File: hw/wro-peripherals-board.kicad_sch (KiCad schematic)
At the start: 0 parts

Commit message: Schematic V1
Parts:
- added J1: I2C Breakout (OLED), symbol Connector:Conn_01x04_Pin
- added J2: Power-Motor Screw Terminal, symbol Connector:Conn_01x06_Pin
- added J3: GY-87 Sensor Breakout, symbol Connector:Conn_01x08_Pin
- added J4: PWM Out, symbol Connector:Conn_01x03_Pin
- added J5: PWM In, symbol Connector:Conn_01x04_Pin
- added U1: Raspberry Pi Pico, Module:RaspberryPi_Pico_Common_Unspecified, symbol MCU_Module:RaspberryPi_Pico
- added U2: TB6612FNG, Package_SO:SSOP-24_5.3x8.2mm_P0.65mm, symbol Driver_Motor:TB6612FNG
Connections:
- new net: J2.3 (Pin_3), U2.1 (AO1), U2.2 (AO1)
- new net: J2.4 (Pin_4), U2.5 (AO2), U2.6 (AO2)
- new net: J2.5 (Pin_5), U2.11 (BO1), U2.12 (BO1)
- new net: J2.6 (Pin_6), U2.7 (BO2), U2.8 (BO2)
- new net +3.3V: J1.2 (Pin_2), U1.36 (3V3), U2.20 (VCC)
- new net +5V: J3.1 (Pin_1), J5.3 (Pin_3), U1.40 (VBUS)
- new net +BATT: J2.1 (Pin_1), J4.2 (Pin_2), U2.13 (VM2), U2.14 (VM3), U2.24 (VM1)
- new net AIN1: U1.15 (GPIO11), U2.21 (AIN1)
- new net AIN2: U1.14 (GPIO10), U2.22 (AIN2)
- new net BIN1: U1.17 (GPIO13), U2.17 (BIN1)
- new net BIN2: U1.19 (GPIO14), U2.16 (BIN2)
- new net GND: J1.1 (Pin_1), J2.2 (Pin_2), J3.3 (Pin_3), J4.3 (Pin_3), J5.4 (Pin_4), U1.13 (GND), U1.18 (GND), U1.23 (GND), U1.28 (GND), U1.3 (GND), U1.38 (GND), U1.8 (GND), U2.10 (PGND2), U2.18 (GND), U2.3 (PGND1), U2.4 (PGND1), U2.9 (PGND2)
- new net PWMA: U1.12 (GPIO9), U2.23 (PWMA)
- new net PWMB: U1.20 (GPIO15), U2.15 (PWMB)
- new net RX_S: J5.2 (Pin_2), U1.22 (GPIO17)
- new net RX_T: J5.1 (Pin_1), U1.24 (GPIO18)
- new net SCL: J1.3 (Pin_3), J3.4 (Pin_4), U1.7 (GPIO5)
- new net SDA: J1.4 (Pin_4), J3.5 (Pin_5), U1.6 (GPIO4)
- new net SERVO: J4.1 (Pin_1), U1.21 (GPIO16)
- new net STBY: U1.16 (GPIO12), U2.19 (STBY)
- no-connect marks 0 -> 4
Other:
- company: (none) -> DIY Labs
- title: (none) -> WRO Peripherals Board 

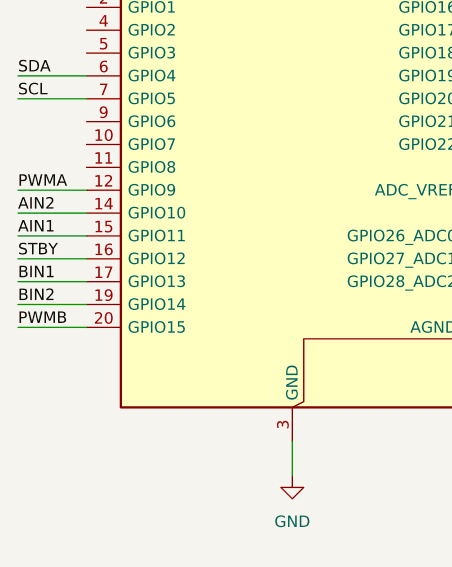
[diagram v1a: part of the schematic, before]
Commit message: Change pinout of motor driver control pins
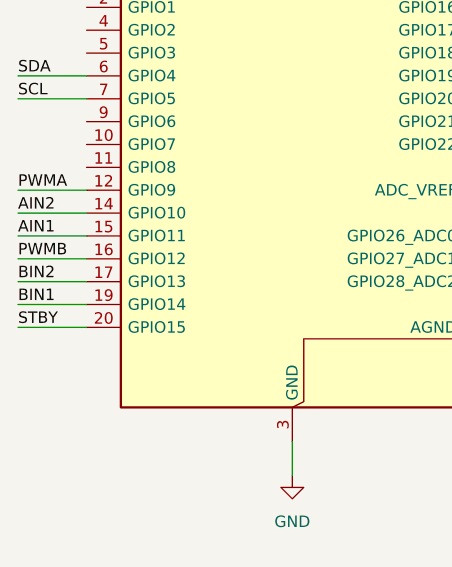
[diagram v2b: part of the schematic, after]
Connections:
- net BIN1: now also U1.19 (GPIO14); no longer U1.17 (GPIO13)
- net BIN2: now also U1.17 (GPIO13); no longer U1.19 (GPIO14)
- net PWMB: now also U1.16 (GPIO12); no longer U1.20 (GPIO15)
- net STBY: now also U1.20 (GPIO15); no longer U1.16 (GPIO12)
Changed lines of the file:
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@@
 		)
 	)
-	(label "STBY"
+	(label "PWMB"
 		(at 35.56 87.63 0)
-		(effects
-			(font
-				(size 1.27 1.27)
-			)
-			(justify left bottom)
-		)
-	)
-	(label "BIN1"
-		(at 35.56 90.17 0)
 		(effects
 			(font
@@
 		)
 	)
-	(label "PWMB"
-		(at 35.56 95.25 0)
+	(label "BIN1"
+		(at 35.56 92.71 0)
 		(effects
 			(font
@@
 		)
 	)
-	(label "BIN2"
-		(at 35.56 92.71 0)
-		(effects
-			(font
-				(size 1.27 1.27)
-			)
-			(justify left bottom)
-		)
-	)
 	(label "SCL"
 		(at 35.56 69.85 0)
@@
 	(label "AIN1"
 		(at 121.92 60.96 0)
+		(effects
+			(font
+				(size 1.27 1.27)
+			)
+			(justify left bottom)
+		)
+	)
+	(label "BIN2"
+		(at 35.56 90.17 0)
 		(effects
 			(font
@@
 		(effects
 			(font
+				(size 1.27 1.27)
+			)
+			(justify left bottom)
+		)
+	)
+	(label "STBY"
+		(at 35.56 95.25 0)
+		(effects
+			(font

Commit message: Update schematic
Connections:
- net RX_S: now also U1.21 (GPIO16); no longer U1.22 (GPIO17)
- net RX_T: now also U1.22 (GPIO17); no longer U1.24 (GPIO18)
- net SERVO: now also U1.24 (GPIO18); no longer U1.21 (GPIO16)
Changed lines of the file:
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@@
+		)
+	)
+	(label "RX_S"
+		(at 96.52 59.69 180)
+		(effects
+			(font
+				(size 1.27 1.27)
+			)
+			(justify right bottom)
 		)
 	)
@@
 		)
 	)
+	(label "RX_T"
+		(at 96.52 62.23 180)
+		(effects
+			(font
+				(size 1.27 1.27)
+			)
+			(justify right bottom)
+		)
+	)
 	(label "SDA"
 		(at 246.38 74.93 180)
@@
 		)
 	)
-	(label "RX_S"
-		(at 96.52 62.23 180)
-		(effects
-			(font
-				(size 1.27 1.27)
-			)
-			(justify right bottom)
-		)
-	)
 	(label "SCL"
 		(at 246.38 48.26 180)
@@
 		)
 	)
+	(label "SERVO"
+		(at 96.52 64.77 180)
+		(effects
+			(font
+				(size 1.27 1.27)
+			)
+			(justify right bottom)
+		)
+	)
 	(label "PWMA"
 		(at 35.56 80.01 0)
@@
 		)
 	)
-	(label "RX_T"
-		(at 96.52 64.77 180)
-		(effects
-			(font
-				(size 1.27 1.27)
-			)
-			(justify right bottom)
-		)
-	)
 	(label "SERVO"
 		(at 246.38 93.98 180)
 		(effects
 			(font
-				(size 1.27 1.27)
-			)
-			(justify right bottom)
-		)
-	)
-	(label "SERVO"
-		(at 96.52 59.69 180)
-		(effects
-			(font
